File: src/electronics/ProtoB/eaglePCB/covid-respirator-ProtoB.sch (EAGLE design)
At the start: 18 parts, among them IC2 L7805CV-DG, Q1 VNP35N07-E, T2 BC548

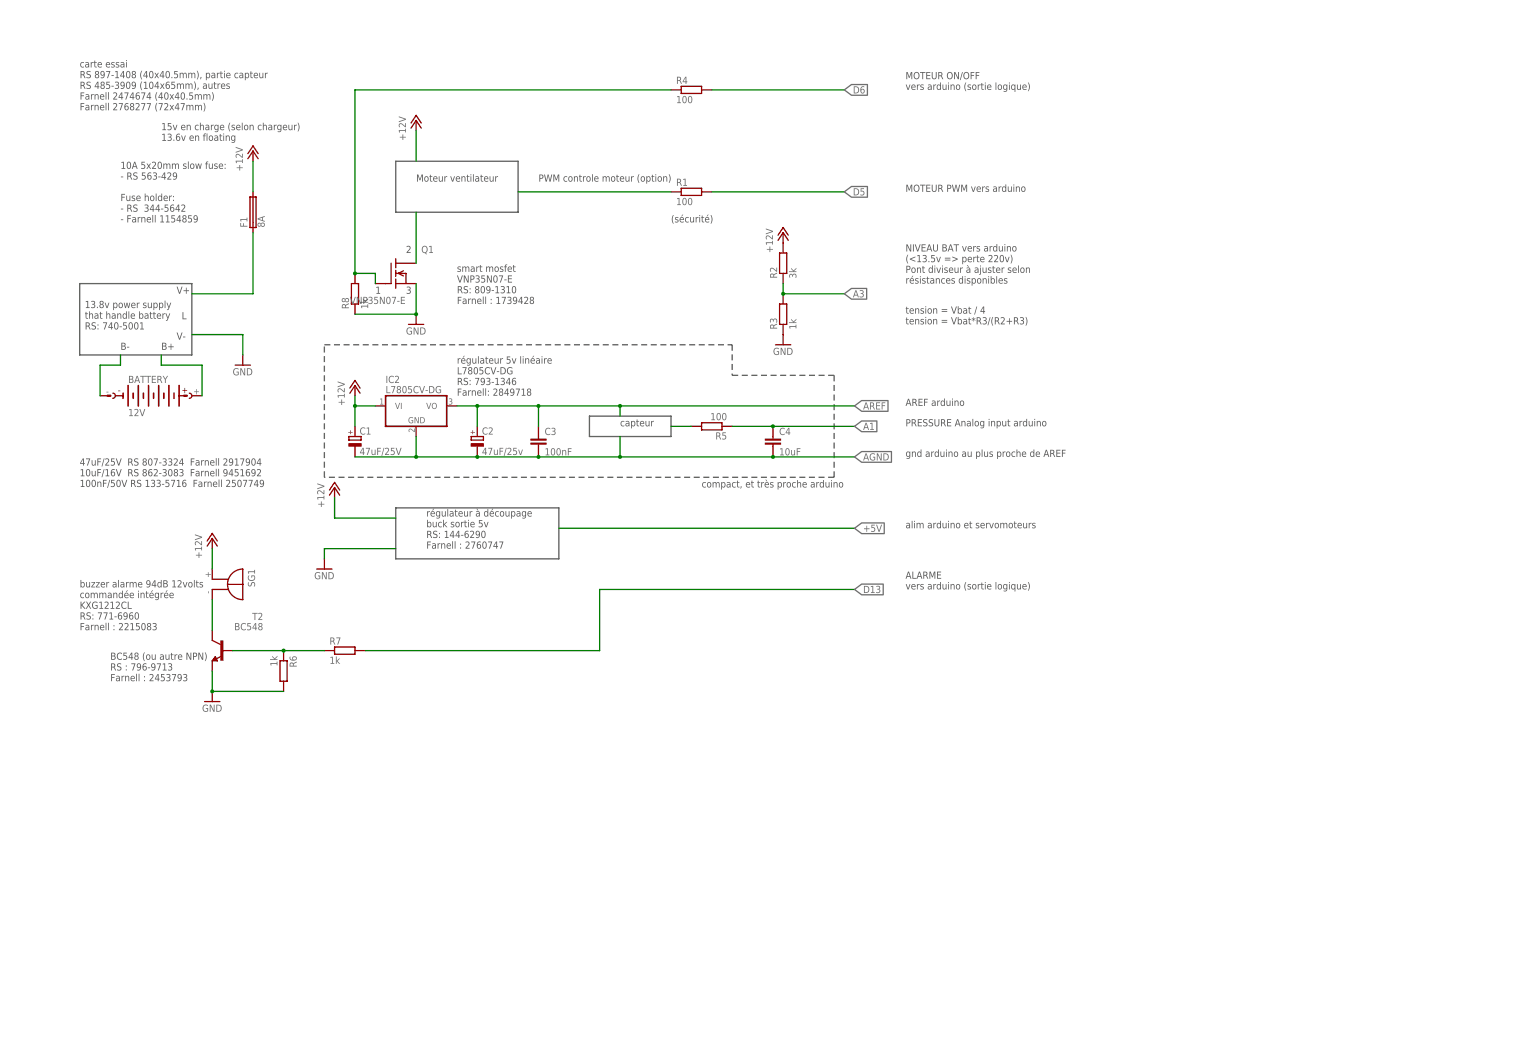
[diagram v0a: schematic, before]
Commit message: update protoB schematic
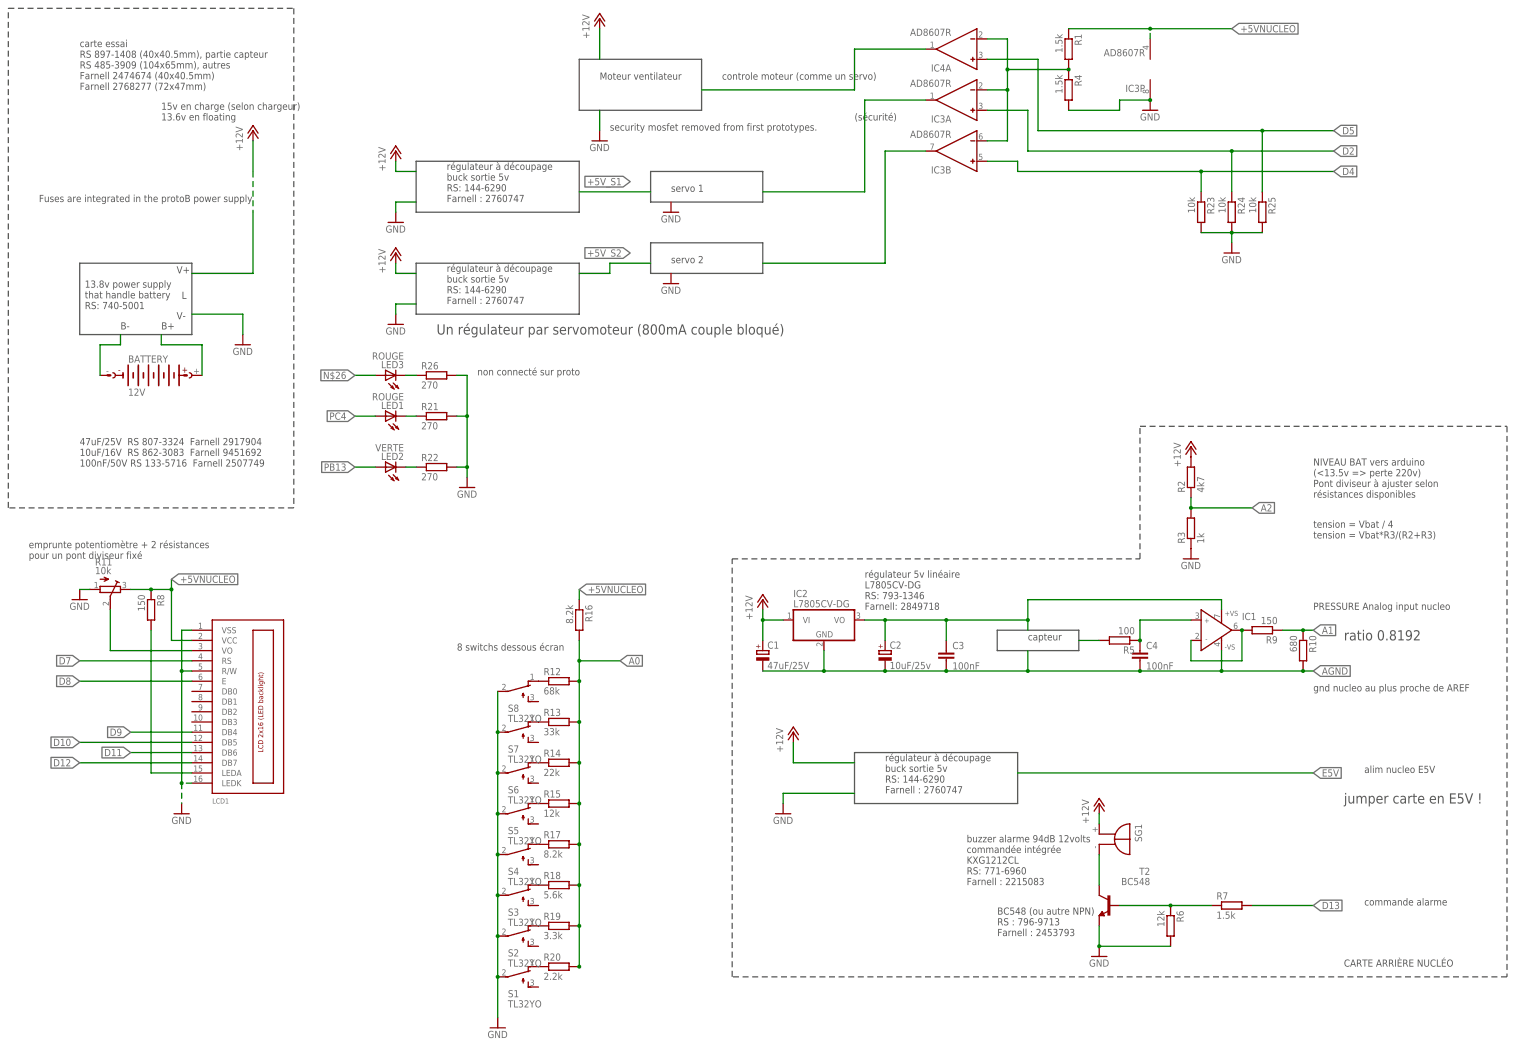
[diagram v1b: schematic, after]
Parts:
- removed F1: 8A, fuse:19560
- removed Q1: VNP35N07-E, transistor-fet:BUZ72
- added IC1: AD825R, analog-devices:AD825R
- added IC3, IC4: AD8607R, analog-devices:AD8607R
- added LCD1: LCD_2X16_SIL, lcd_2x16_led_backlight:LCD_2X16_SIL
- added LED1, LED3: ROUGE, led:LED3MM
- added LED2: VERTE, led:LED3MM
- added R10: 680, rcl:R-EU_0207/10
- added R11: 10k, pot:TRIM_EU-SM-42/43B
- added R12: 68k, rcl:R-EU_0207/10
- added R13: 33k, rcl:R-EU_0207/10
- added R14: 22k, rcl:R-EU_0207/10
- added R15: 12k, rcl:R-EU_0207/10
- added R16, R17: 8.2k, rcl:R-EU_0207/10
- added R18: 5.6k, rcl:R-EU_0207/10
- added R19: 3.3k, rcl:R-EU_0207/10
- added R20: 2.2k, rcl:R-EU_0207/10
- added R21, R22, R26: 270, rcl:R-EU_0207/10
- added R23, R24, R25: 10k, rcl:R-EU_0207/10
- added R9: 150, rcl:R-EU_0207/10
- added S1, S2, S3, S4, S5, S6, S7, S8: TL32YO, switch:TL32YO
- C2: value 47uF/25v -> 10uF/25v
- C4: value 10uF -> 100nF
- R1, R4: value 100 -> 1.5k
- R2: value 3k -> 4k7
- R6: value 1k -> 12k
- R7: value 1k -> 1.5k
- R8: value 1k -> 150
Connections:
- net A3 renamed A2
- removed net D6: R4.2
- new net +5VNUCLEO: IC3P.V-, LCD1.VCC, R1.1, R11.E, R16.1, R8.1
- new net 6546876: C4.1, IC1.IN+, R5.1
- new net A0: R12.2, R13.2, R14.2, R15.2, R16.2, R17.2, R18.2, R19.2, R20.2
- new net D10: LCD1.DB5
- new net D11: LCD1.DB6
- new net D12: LCD1.DB7
- new net D2: IC3A.IN+, R24.1
- new net D4: IC3B.IN+, R23.1
- new net D7: LCD1.RS
- new net D8: LCD1.E
- new net D9: LCD1.DB4
- new net N$10: LCD1.VO, R11.S
- new net N$11: R12.1, S8.O
- new net N$14: R13.1, S7.O
- new net N$15: R14.1, S6.O
- new net N$16: R15.1, S5.O
- new net N$18: R17.1, S4.O
- new net N$19: R18.1, S3.O
- new net N$20: R19.1, S2.O
- new net N$21: R20.1, S1.O
- new net N$22: LED3.C, R26.1
- new net N$23: LED1.C, R21.1
- new net N$24: LED2.C, R22.1
- new net N$26: LED3.A
- new net N$7: LCD1.LEDA, R8.2
- new net N$8: IC1.IN-, IC1.OUT, R9.2
- new net PB13: LED2.A
- new net PC4: LED1.A
- net +12V: no longer F1.2
- net A1: now also R10.1, R9.1; no longer C4.1, R5.1
- net AGND: now also IC1.-VS, R10.2
- net AREF: now also IC1.+VS
- net D5: now also IC4A.IN+, R25.1; no longer R1.2
- net GND: now also IC3P.V+, LCD1.LEDK, LCD1.R/W, LCD1.VSS, R11.A, R21.2, R22.2, R23.2, R24.2, R25.2, R26.2, R4.2, S1.P, S2.P, S3.P, S4.P, S5.P, S6.P, S7.P, S8.P; no longer Q1.S, R8.1
- net N$1: now also IC4A.OUT; no longer R1.1
- net N$4: now also IC3A.IN-, IC3B.IN-, IC4A.IN-, R1.2, R4.1; no longer Q1.D
- net N$5: now also IC3A.OUT; no longer F1.1
- net N$6: now also IC3B.OUT; no longer Q1.G, R4.1, R8.2
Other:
- note added: "8 switchs dessous écran"
- note added: "CARTE ARRIÈRE NUCLÉO"
- note added: "Fuses are integrated in the protoB power supply"
- note added: "PRESSURE Analog input nucleo"
- note added: "Un régulateur par servomoteur (800mA couple bloqué)"
- note added: "alim nucleo E5V"
- note added: "commande alarme"
- note added: "controle moteur (comme un servo)"
- note added: "emprunte potentiomètre + 2 résistances pour un pont diviseur fixé"
- note added: "gnd nucleo au plus proche de AREF"
- note added: "jumper carte en E5V !"
- note added: "non connecté sur proto"
- note added: "ratio 0.8192"
- note added: "security mosfet removed from first prototypes."
- note added: "servo 1"
- note added: "servo 2"
- note removed: "1"
- note removed: "10A 5x20mm slow fuse: - RS 563-429 Fuse holder: - RS 344-5642 - Farnell 1154859"
- note removed: "2"
- note removed: "3"
- note removed: "ALARME vers arduino (sortie logique)"
- note removed: "AREF arduino"
- note removed: "MOTEUR ON/OFF vers arduino (sortie logique)"
- note removed: "MOTEUR PWM vers arduino"
- note removed: "PRESSURE Analog input arduino"
- note removed: "PWM controle moteur (option)"
- note removed: "alim arduino et servomoteurs"
- note removed: "compact, et très proche arduino"
- note removed: "gnd arduino au plus proche de AREF"
- note removed: "smart mosfet VNP35N07-E RS: 809-1310 Farnell : 1739428"
- moved on the sheet: BATTERY, C1, C2, C3, C4, IC2, R1, R2, R3, R4, R5, R6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
